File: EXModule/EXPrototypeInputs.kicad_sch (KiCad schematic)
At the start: 6 parts

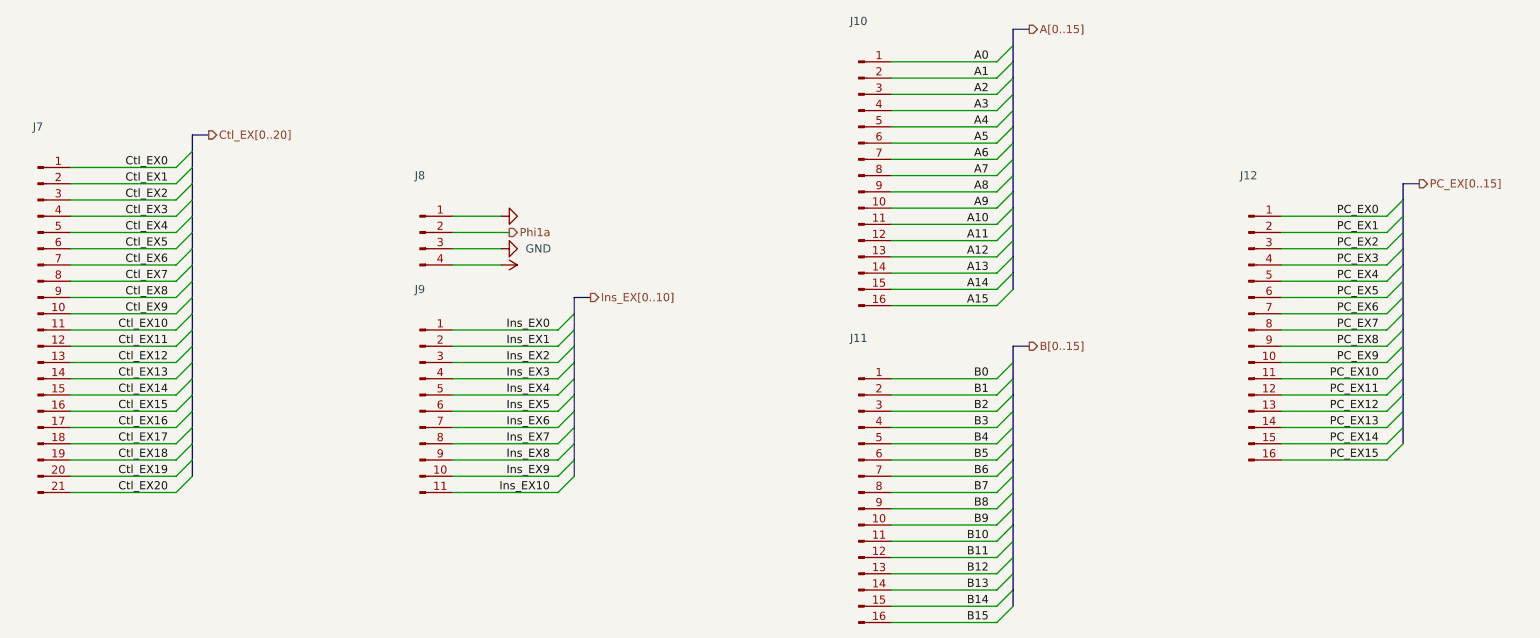
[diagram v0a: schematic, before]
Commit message: Fix clock inputs on schematic for EX
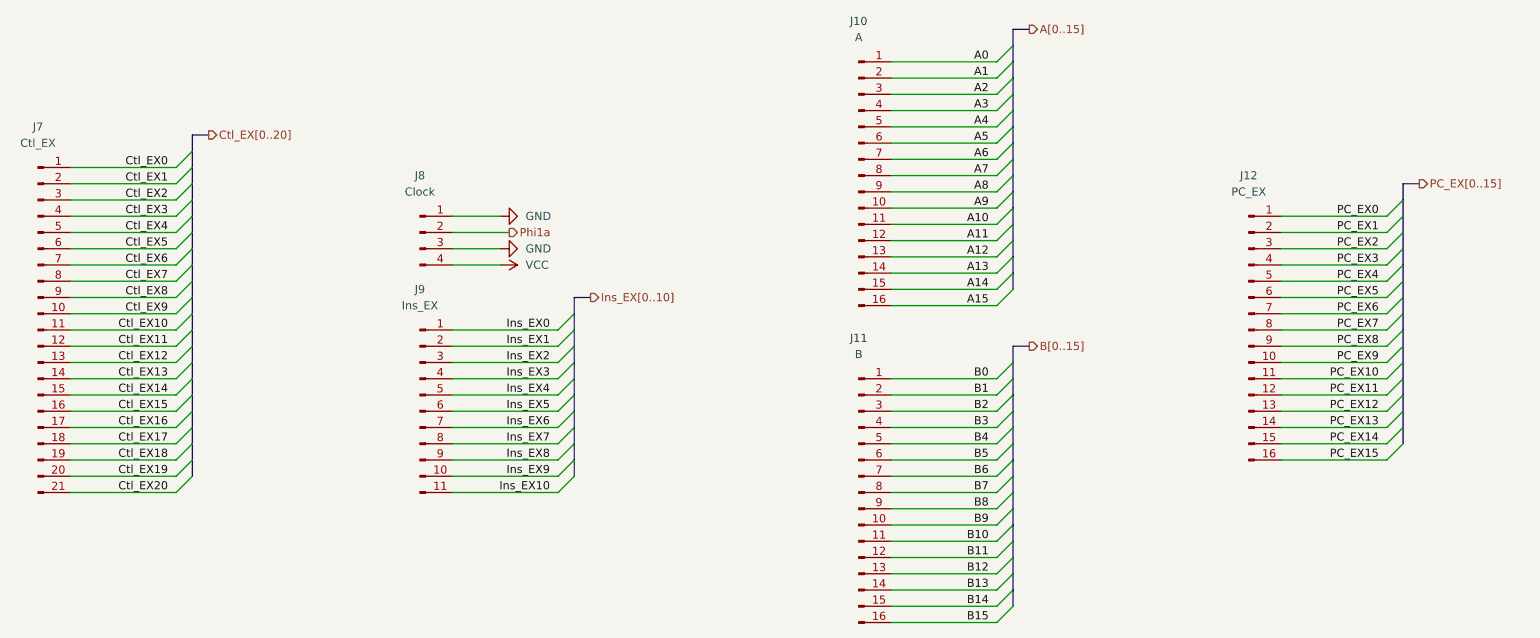
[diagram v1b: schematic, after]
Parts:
- J10: value (none) -> A
- J11: value (none) -> B
- J12: value (none) -> PC_EX
- J7: value (none) -> Ctl_EX; footprint (none) -> Connector_PinHeader_2.54mm:PinHeader_1x21_P2.54mm_Vertical
- J8: value (none) -> Clock; footprint (none) -> Connector_PinHeader_2.54mm:PinHeader_1x04_P2.54mm_Vertical
- J9: value (none) -> Ins_EX; footprint (none) -> Connector_PinHeader_2.54mm:PinHeader_1x11_P2.54mm_Vertical
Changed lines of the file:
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@@
     (title "Turtle16: EX Module Inputs")
     (date "2022-04-12")
-    (rev "A")
+    (rev "A (7b9791c7)")
   )
   (bus_entry (at 190.5 66.04) (size -2.54 2.54)
@@
     (in_bom yes) (on_board yes)
     (property "Reference" "J11" (id 0) (at 166.37 104.14 0))
-    (property "Value" "" (id 1) (at 166.37 106.68 0))
+    (property "Value" "B" (id 1) (at 166.37 106.68 0))
     (property "Footprint" "Connector_PinHeader_2.54mm:PinHeader_1x16_P2.54mm_Vertical" (id 2) (at 166.37 128.27 0)
       (effects (font (size 1.27 1.27)) hide)
@@
     (in_bom yes) (on_board yes)
     (property "Reference" "J12" (id 0) (at 227.33 78.74 0))
-    (property "Value" "" (id 1) (at 227.33 81.28 0))
+    (property "Value" "PC_EX" (id 1) (at 227.33 81.28 0))
     (property "Footprint" "Connector_PinHeader_2.54mm:PinHeader_1x16_P2.54mm_Vertical" (id 2) (at 227.33 102.87 0)
       (effects (font (size 1.27 1.27)) hide)
@@
     (in_bom yes) (on_board yes)
     (property "Reference" "J8" (id 0) (at 97.79 78.74 0))
-    (property "Value" "" (id 1) (at 97.79 81.28 0))
-    (property "Footprint" "" (id 2) (at 97.79 87.63 0)
+    (property "Value" "Clock" (id 1) (at 97.79 81.28 0))
+    (property "Footprint" "Connector_PinHeader_2.54mm:PinHeader_1x04_P2.54mm_Vertical" (id 2) (at 97.79 87.63 0)
       (effects (font (size 1.27 1.27)) hide)
     )
@@
       (effects (font (size 1.27 1.27)) hide)
     )
-    (property "Value" "" (id 1) (at 114.3 92.7099 90)
+    (property "Value" "VCC" (id 1) (at 114.3 92.7099 90)
       (effects (font (size 1.27 1.27)) (justify left))
     )
@@
     (in_bom yes) (on_board yes)
     (property "Reference" "J10" (id 0) (at 166.37 54.61 0))
-    (property "Value" "" (id 1) (at 166.37 57.15 0))
+    (property "Value" "A" (id 1) (at 166.37 57.15 0))
     (property "Footprint" "Connector_PinHeader_2.54mm:PinHeader_1x16_P2.54mm_Vertical" (id 2) (at 166.37 78.74 0)
       (effects (font (size 1.27 1.27)) hide)
@@
     (in_bom yes) (on_board yes)
     (property "Reference" "J9" (id 0) (at 97.79 96.52 0))
-    (property "Value" "" (id 1) (at 97.79 99.06 0))
-    (property "Footprint" "" (id 2) (at 97.79 115.57 0)
+    (property "Value" "Ins_EX" (id 1) (at 97.79 99.06 0))
+    (property "Footprint" "Connector_PinHeader_2.54mm:PinHeader_1x11_P2.54mm_Vertical" (id 2) (at 97.79 115.57 0)
       (effects (font (size 1.27 1.27)) hide)
     )
@@
     (in_bom yes) (on_board yes)
     (property "Reference" "J7" (id 0) (at 38.1 71.12 0))
-    (property "Value" "" (id 1) (at 38.1 73.66 0))
-    (property "Footprint" "" (id 2) (at 38.1 102.87 0)
+    (property "Value" "Ctl_EX" (id 1) (at 38.1 73.66 0))
+    (property "Footprint" "Connector_PinHeader_2.54mm:PinHeader_1x21_P2.54mm_Vertical" (id 2) (at 38.1 102.87 0)
       (effects (font (size 1.27 1.27)) hide)
     )
@@
       (effects (font (size 1.27 1.27)) hide)
     )
-    (property "Value" "" (id 1) (at 114.3 85.0899 90)
+    (property "Value" "GND" (id 1) (at 114.3 85.0899 90)
       (effects (font (size 1.27 1.27)) (justify right))
     )

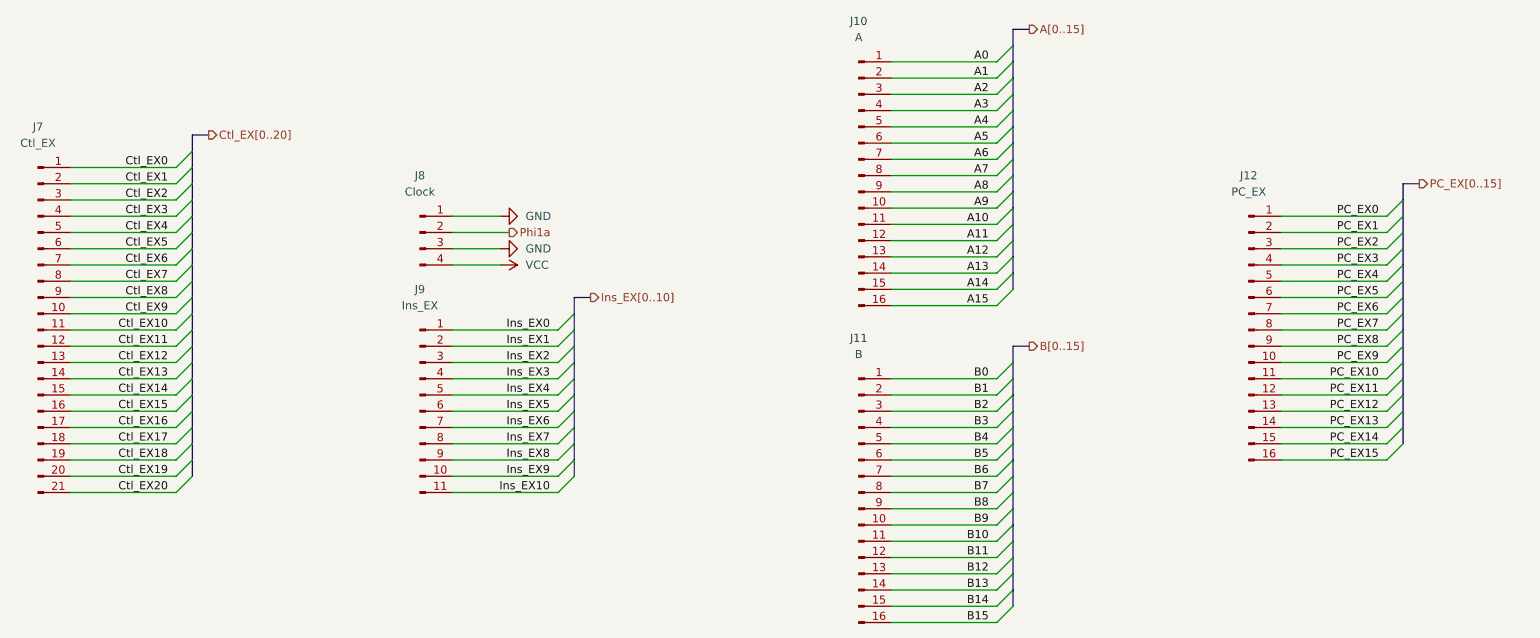
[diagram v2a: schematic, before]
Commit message: Change module PCB layouts for better integration
Modules will be connected to one another and so it's useful to rearrange
the input and output headers to make the wiring easier and cleaner. This
may mean that PCBs are larger than necessary and contain more dead space.
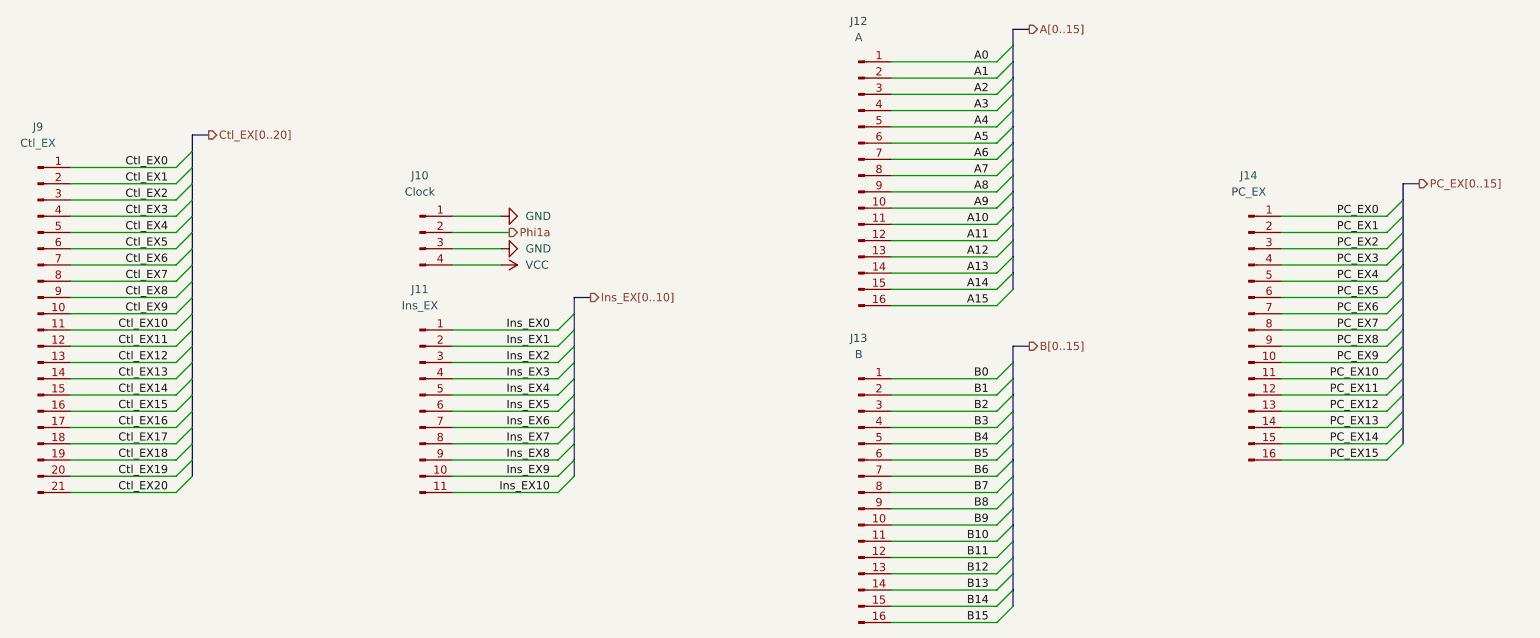
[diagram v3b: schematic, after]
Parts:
- renumbered J8 to J10, J9 to J11, J10 to J12, J11 to J13, J12 to J14, J7 to J9
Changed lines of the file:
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@@
   (symbol (lib_id "Connector:Conn_01x16_Male") (at 166.37 128.27 0) (unit 1)
     (in_bom yes) (on_board yes)
-    (property "Reference" "J11" (id 0) (at 166.37 104.14 0))
+    (property "Reference" "J13" (id 0) (at 166.37 104.14 0))
     (property "Value" "B" (id 1) (at 166.37 106.68 0))
     (property "Footprint" "Connector_PinHeader_2.54mm:PinHeader_1x16_P2.54mm_Vertical" (id 2) (at 166.37 128.27 0)
@@
   (symbol (lib_id "Connector:Conn_01x16_Male") (at 227.33 102.87 0) (unit 1)
     (in_bom yes) (on_board yes)
-    (property "Reference" "J12" (id 0) (at 227.33 78.74 0))
+    (property "Reference" "J14" (id 0) (at 227.33 78.74 0))
     (property "Value" "PC_EX" (id 1) (at 227.33 81.28 0))
     (property "Footprint" "Connector_PinHeader_2.54mm:PinHeader_1x16_P2.54mm_Vertical" (id 2) (at 227.33 102.87 0)
@@
   (symbol (lib_id "Connector:Conn_01x04_Male") (at 97.79 87.63 0) (unit 1)
     (in_bom yes) (on_board yes)
-    (property "Reference" "J8" (id 0) (at 97.79 78.74 0))
+    (property "Reference" "J10" (id 0) (at 97.79 78.74 0))
     (property "Value" "Clock" (id 1) (at 97.79 81.28 0))
     (property "Footprint" "Connector_PinHeader_2.54mm:PinHeader_1x04_P2.54mm_Vertical" (id 2) (at 97.79 87.63 0)
@@
   (symbol (lib_id "Connector:Conn_01x16_Male") (at 166.37 78.74 0) (unit 1)
     (in_bom yes) (on_board yes)
-    (property "Reference" "J10" (id 0) (at 166.37 54.61 0))
+    (property "Reference" "J12" (id 0) (at 166.37 54.61 0))
     (property "Value" "A" (id 1) (at 166.37 57.15 0))
     (property "Footprint" "Connector_PinHeader_2.54mm:PinHeader_1x16_P2.54mm_Vertical" (id 2) (at 166.37 78.74 0)
@@
   (symbol (lib_id "Connector:Conn_01x11_Male") (at 97.79 115.57 0) (unit 1)
     (in_bom yes) (on_board yes)
-    (property "Reference" "J9" (id 0) (at 97.79 96.52 0))
+    (property "Reference" "J11" (id 0) (at 97.79 96.52 0))
     (property "Value" "Ins_EX" (id 1) (at 97.79 99.06 0))
     (property "Footprint" "Connector_PinHeader_2.54mm:PinHeader_1x11_P2.54mm_Vertical" (id 2) (at 97.79 115.57 0)
@@
   (symbol (lib_id "Connector:Conn_01x21_Male") (at 38.1 102.87 0) (unit 1)
     (in_bom yes) (on_board yes)
-    (property "Reference" "J7" (id 0) (at 38.1 71.12 0))
+    (property "Reference" "J9" (id 0) (at 38.1 71.12 0))
     (property "Value" "Ctl_EX" (id 1) (at 38.1 73.66 0))
     (property "Footprint" "Connector_PinHeader_2.54mm:PinHeader_1x21_P2.54mm_Vertical" (id 2) (at 38.1 102.87 0)
